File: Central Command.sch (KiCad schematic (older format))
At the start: 16 parts, among them P1 CONN_01X06, P2 CONN_01X02, U1 STM32F030C8, U2 MCP1700T-3302E/TT_

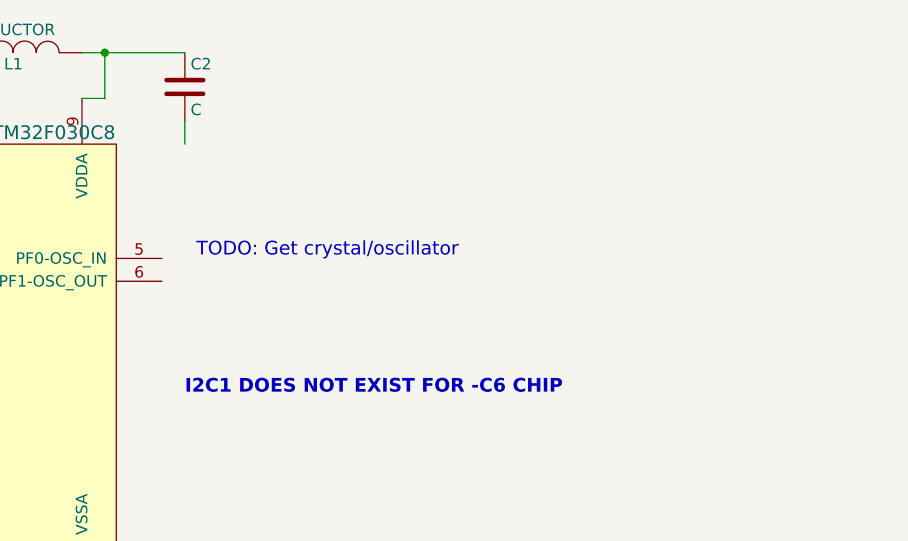
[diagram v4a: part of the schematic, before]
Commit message: Added Crystal to the schematic and layout
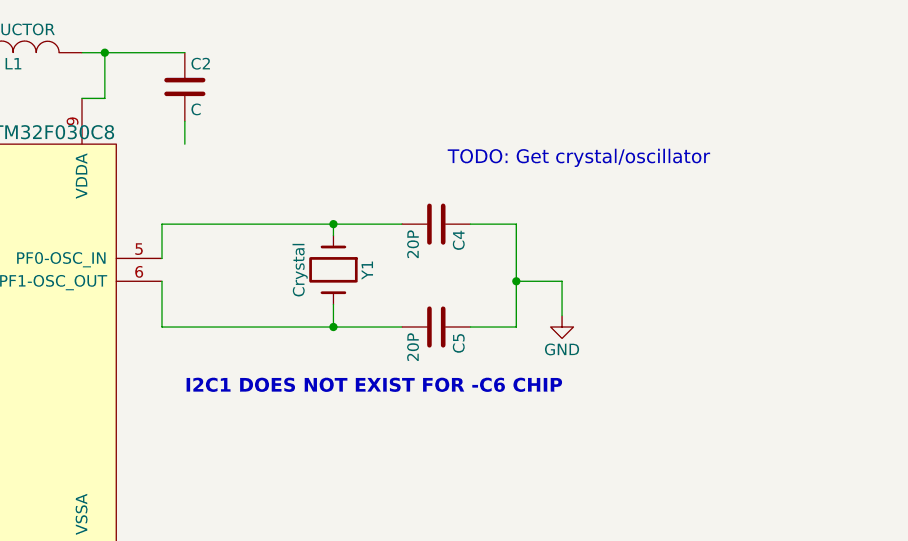
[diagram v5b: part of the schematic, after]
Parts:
- added C4, C5: 20P, Capacitors_SMD:C_0805, symbol C
- added Y1: Crystal, Crystals:Crystal_HC49-U_Vertical, symbol Crystal
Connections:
- wire segments 57 -> 68
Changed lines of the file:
@@
 	-1   0    0    -1
 $EndComp
-Wire Wire Line
-	7550 800  8000 800
-Wire Wire Line
-	7550 1000 7650 1000
-Wire Wire Line
-	7650 1000 7650 800
-Connection ~ 7650 800
-Wire Wire Line
-	8000 1100 8000 1200
-Wire Wire Line
-	6300 800  6950 800
-Wire Wire Line
-	6700 800  6700 1000
-Wire Wire Line
-	6800 800  6800 1000
-Connection ~ 6800 800
-Wire Wire Line
-	6900 1000 6900 900
-Wire Wire Line
-	6900 900  6800 900
-Connection ~ 6800 900
-Wire Wire Line
-	9050 4850 9050 5200
-Wire Wire Line
-	9050 5000 10150 5000
-Wire Wire Line
-	10150 5000 10150 4650
-Connection ~ 9050 5000
-Wire Wire Line
-	9050 5100 7900 5100
-Wire Wire Line
-	7900 5100 7900 4600
-Connection ~ 9050 5100
-Wire Wire Line
-	7300 4050 8300 4050
-Wire Wire Line
-	7900 4300 7900 4050
-Wire Wire Line
-	7900 4050 7950 4050
-Connection ~ 7950 4050
-Wire Wire Line
-	9800 4050 10600 4050
-Wire Wire Line
-	10150 4050 10150 4350
-Connection ~ 10150 4050
-Wire Wire Line
-	10750 4100 10600 4100
-Wire Wire Line
-	10600 4100 10600 4050
-Connection ~ 6700 800
-Wire Wire Line
-	6800 3150 6800 3300
-Wire Wire Line
-	6800 3250 7550 3250
-Wire Wire Line
-	6900 3250 6900 3150
-Connection ~ 6800 3250
-Wire Wire Line
-	7550 3250 7550 3150
-Connection ~ 6900 3250
-Wire Wire Line
-	5200 2500 6100 2500
-Wire Wire Line
-	5700 2500 5700 2600
-Wire Wire Line
-	5700 2900 5700 3100
-Wire Wire Line
-	5450 2600 5450 2500
-Connection ~ 5700 2500
-Wire Wire Line
-	5200 2600 5200 2500
-Connection ~ 5450 2500
-Wire Wire Line
-	1500 2500 3050 2500
-Wire Wire Line
-	1500 2500 1500 2800
-Wire Wire Line
-	1500 2800 750  2800
 Text GLabel 1900 1900 2    60   Input ~ 0
 3V3
-Wire Wire Line
-	850  1900 1900 1900
-Wire Wire Line
-	850  1900 850  2100
 $Comp
 L R R2
@@
 	1    0    0    -1
 $EndComp
-Wire Wire Line
-	850  2400 850  2500
-Wire Wire Line
-	850  2500 750  2500
 $Comp
 L GND #PWR03
@@
 	1    0    0    -1
 $EndComp
-Wire Wire Line
-	1000 2700 1000 3200
-Wire Wire Line
-	1000 2700 750  2700
-Wire Wire Line
-	750  2900 850  2900
-Wire Wire Line
-	850  2900 850  3600
 Text GLabel 1050 3600 2    60   Input ~ 0
 NRST
-Wire Wire Line
-	850  3600 1050 3600
 Text GLabel 6100 2850 0    60   Input ~ 0
 NRST
-Wire Wire Line
-	6100 2650 6100 2850
 $Comp
 L R R4
@@
 	1    0    0    -1
 $EndComp
-Wire Wire Line
-	1650 2400 1650 2500
-Connection ~ 1650 2500
-Wire Wire Line
-	1650 2100 1650 1900
-Connection ~ 1650 1900
-Wire Wire Line
-	1850 3050 1850 3150
-Wire Wire Line
-	1850 3150 1000 3150
-Connection ~ 1000 3150
-Wire Wire Line
-	1850 2600 1850 2750
-Wire Wire Line
-	750  2600 3050 2600
-Connection ~ 1850 2600
 $Comp
 L R R1
@@
 	1    0    0    -1
 $EndComp
-Wire Wire Line
-	750  3200 750  3000
-Wire Wire Line
-	750  3500 750  4000
-Wire Wire Line
-	750  4000 1050 4000
 Text GLabel 1050 4000 2    60   Input ~ 0
 TRACE
@@
 	0    1    1    0
 $EndComp
-Wire Wire Line
-	2850 2000 3050 2000
 $Comp
 L CONN_01X02 P2
@@
 	-1   0    0    -1
 $EndComp
-Wire Wire Line
-	2550 2000 2550 1400
-Wire Wire Line
-	2550 1400 2200 1400
-Wire Wire Line
-	2200 1500 2350 1500
-Wire Wire Line
-	2350 1500 2350 1650
 $Comp
 L GND #PWR04
@@
 	1    0    0    -1
 $EndComp
-Text Notes 8050 1700 0    60   ~ 0
+Text Notes 9150 1300 0    60   ~ 0
 TODO: Get crystal/oscillator
 Text Notes 2550 3100 0    60   ~ 0
@@
 Text Notes 5150 5700 0    60   ~ 0
 TODO: Determine if USB could be used for serial comm (ask Ron)
+$Comp
+L Crystal Y1
+U 1 1 56529888
+P 8650 1750
+F 0 "Y1" H 8650 1900 50  0000 C CNN
+F 1 "Crystal" H 8650 1600 50  0000 C CNN
+F 2 "Crystals:Crystal_HC49-U_Vertical" H 8650 1750 60  0001 C CNN
+F 3 "" H 8650 1750 60  0000 C CNN
+F 4 "http://parts.io/detail/343558/FOXSLF%2F080-20" H 8650 1750 60  0001 C CNN "Link"
+	1    8650 1750
+	0    1    1    0
+$EndComp
+$Comp
+L C C4
+U 1 1 5652990D
+P 9100 1550
+F 0 "C4" H 9125 1650 50  0000 L CNN
+F 1 "20P" H 9125 1450 50  0000 L CNN
+F 2 "Capacitors_SMD:C_0805" H 9138 1400 30  0001 C CNN
+F 3 "" H 9100 1550 60  0000 C CNN
+	1    9100 1550
+	0    1    1    0
+$EndComp
+$Comp
+L C C5
+U 1 1 56529966
+P 9100 2000
+F 0 "C5" H 9125 2100 50  0000 L CNN
+F 1 "20P" H 9125 1900 50  0000 L CNN
+F 2 "Capacitors_SMD:C_0805" H 9138 1850 30  0001 C CNN
+F 3 "" H 9100 2000 60  0000 C CNN
+	1    9100 2000
+	0    1    1    0
+$EndComp
+$Comp
+L GND #PWR05
+U 1 1 56529BFD
+P 9650 1950
+F 0 "#PWR05" H 9650 1700 50  0001 C CNN
+F 1 "GND" H 9650 1800 50  0000 C CNN
+F 2 "" H 9650 1950 60  0000 C CNN
+F 3 "" H 9650 1950 60  0000 C CNN
+	1    9650 1950
+	1    0    0    -1
+$EndComp
+Wire Wire Line
+	7550 800  8000 800
+Wire Wire Line
+	7550 1000 7650 1000
+Wire Wire Line
+	7650 1000 7650 800
+Connection ~ 7650 800
+Wire Wire Line
+	8000 1100 8000 1200
+Wire Wire Line
+	6300 800  6950 800
+Wire Wire Line
+	6700 800  6700 1000
+Wire Wire Line
+	6800 800  6800 1000
+Connection ~ 6800 800
+Wire Wire Line
+	6900 1000 6900 900
+Wire Wire Line
+	6900 900  6800 900
+Connection ~ 6800 900
+Wire Wire Line
+	9050 4850 9050 5200
+Wire Wire Line
+	9050 5000 10150 5000
+Wire Wire Line
+	10150 5000 10150 4650
+Connection ~ 9050 5000
+Wire Wire Line
+	9050 5100 7900 5100
+Wire Wire Line
+	7900 5100 7900 4600
+Connection ~ 9050 5100
+Wire Wire Line
+	7300 4050 8300 4050
+Wire Wire Line
+	7900 4300 7900 4050
+Wire Wire Line
+	7900 4050 7950 4050
+Connection ~ 7950 4050
+Wire Wire Line
+	9800 4050 10600 4050
+Wire Wire Line
+	10150 4050 10150 4350
+Connection ~ 10150 4050
+Wire Wire Line
+	10750 4100 10600 4100
+Wire Wire Line
+	10600 4100 10600 4050
+Connection ~ 6700 800
+Wire Wire Line
+	6800 3150 6800 3300
+Wire Wire Line
+	6800 3250 7550 3250
+Wire Wire Line
+	6900 3250 6900 3150
+Connection ~ 6800 3250
+Wire Wire Line
+	7550 3250 7550 3150
+Connection ~ 6900 3250
+Wire Wire Line
+	5200 2500 6100 2500
+Wire Wire Line
+	5700 2500 5700 2600
+Wire Wire Line
+	5700 2900 5700 3100
+Wire Wire Line
+	5450 2600 5450 2500
+Connection ~ 5700 2500
+Wire Wire Line
+	5200 2600 5200 2500
+Connection ~ 5450 2500
+Wire Wire Line
+	1500 2500 3050 2500
+Wire Wire Line
+	1500 2500 1500 2800
+Wire Wire Line
+	1500 2800 750  2800
+Wire Wire Line
+	850  1900 1900 1900
+Wire Wire Line
+	850  1900 850  2100
+Wire Wire Line
+	850  2400 850  2500
+Wire Wire Line
+	850  2500 750  2500
+Wire Wire Line
+	1000 2700 1000 3200
+Wire Wire Line
+	1000 2700 750  2700
+Wire Wire Line
+	750  2900 850  2900
+Wire Wire Line
+	850  2900 850  3600
+Wire Wire Line
+	850  3600 1050 3600
+Wire Wire Line
+	6100 2650 6100 2850
+Wire Wire Line
+	1650 2400 1650 2500
+Connection ~ 1650 2500
+Wire Wire Line
+	1650 2100 1650 1900
+Connection ~ 1650 1900
+Wire Wire Line
+	1850 3050 1850 3150
+Wire Wire Line
+	1850 3150 1000 3150
+Connection ~ 1000 3150
+Wire Wire Line
+	1850 2600 1850 2750
+Wire Wire Line
+	750  2600 3050 2600
+Connection ~ 1850 2600
+Wire Wire Line
+	750  3200 750  3000
+Wire Wire Line
+	750  3500 750  4000
+Wire Wire Line
+	750  4000 1050 4000
+Wire Wire Line
+	2850 2000 3050 2000
+Wire Wire Line
+	2550 2000 2550 1400
+Wire Wire Line
+	2550 1400 2200 1400
+Wire Wire Line
+	2200 1500 2350 1500
+Wire Wire Line
+	2350 1500 2350 1650
+Wire Wire Line
+	8950 1550 7900 1550
+Wire Wire Line
+	7900 1550 7900 1700
+Wire Wire Line
+	8650 1600 8650 1550
+Connection ~ 8650 1550
+Wire Wire Line
+	9250 1550 9450 1550
+Wire Wire Line
+	9450 1550 9450 2000
+Wire Wire Line
+	9450 2000 9250 2000
+Wire Wire Line
+	9450 1800 9650 1800
+Wire Wire Line
+	9650 1800 9650 1950
+Connection ~ 9450 1800
+Wire Wire Line
+	8950 2000 7900 2000
+Wire Wire Line
+	7900 2000 7900 1800
+Wire Wire Line
+	8650 1900 8650 2000
+Connection ~ 8650 2000
 $EndSCHEMATC

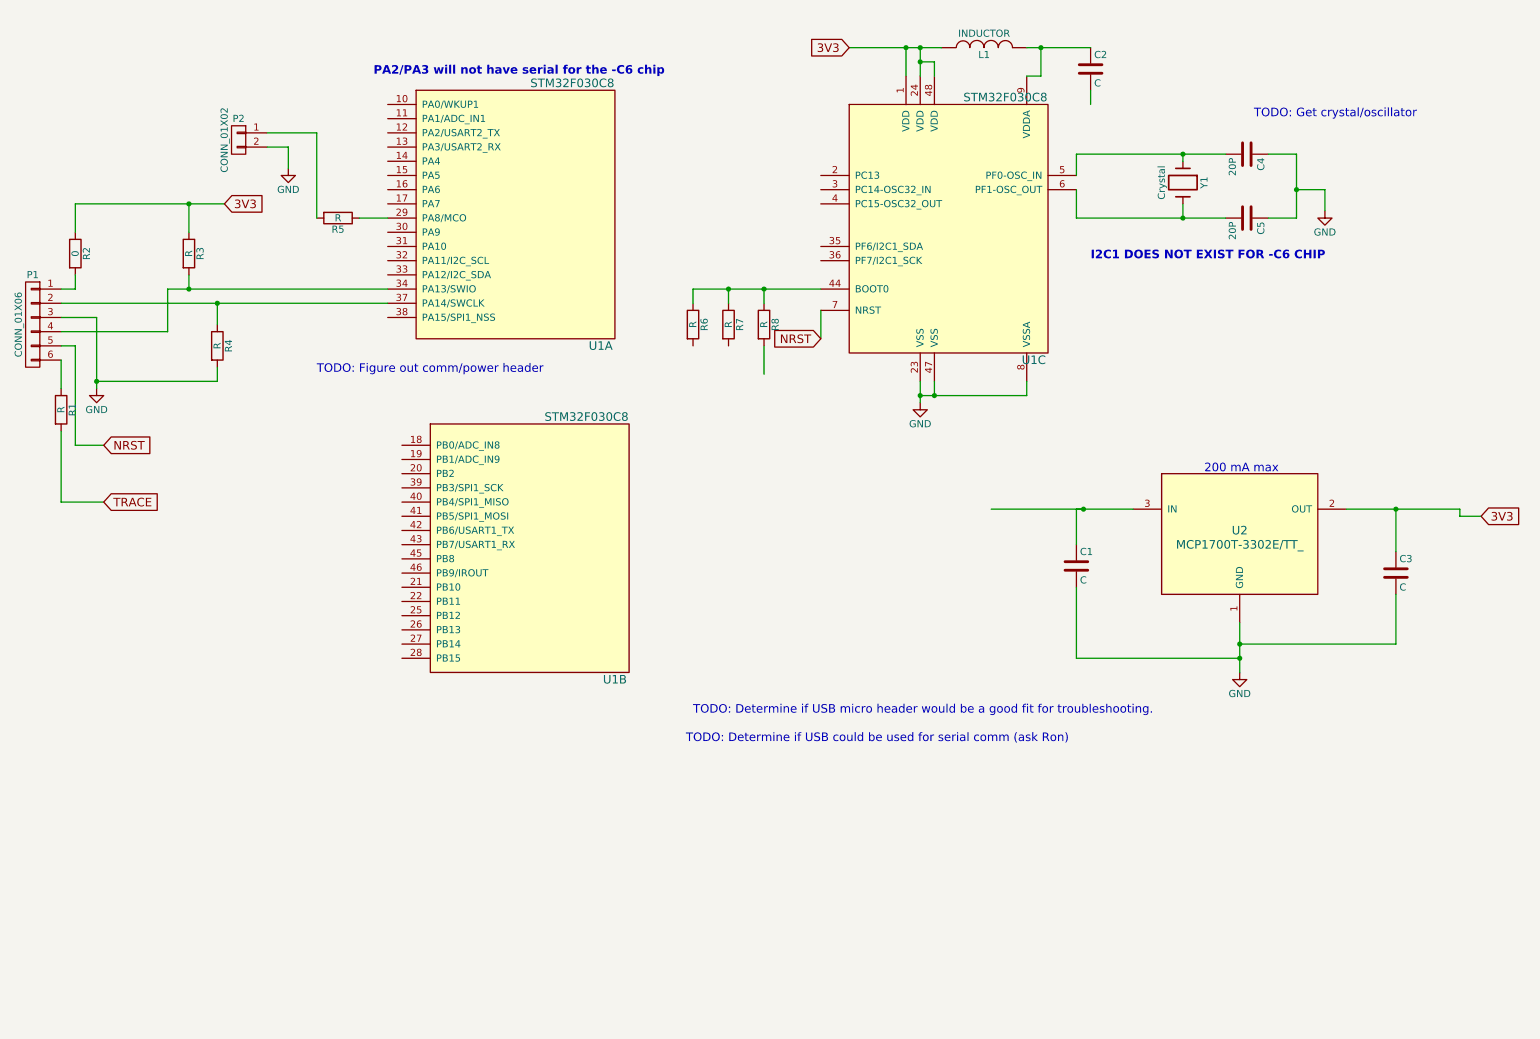
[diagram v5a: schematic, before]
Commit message: Changed BOOT0 pin hookup, added reset button
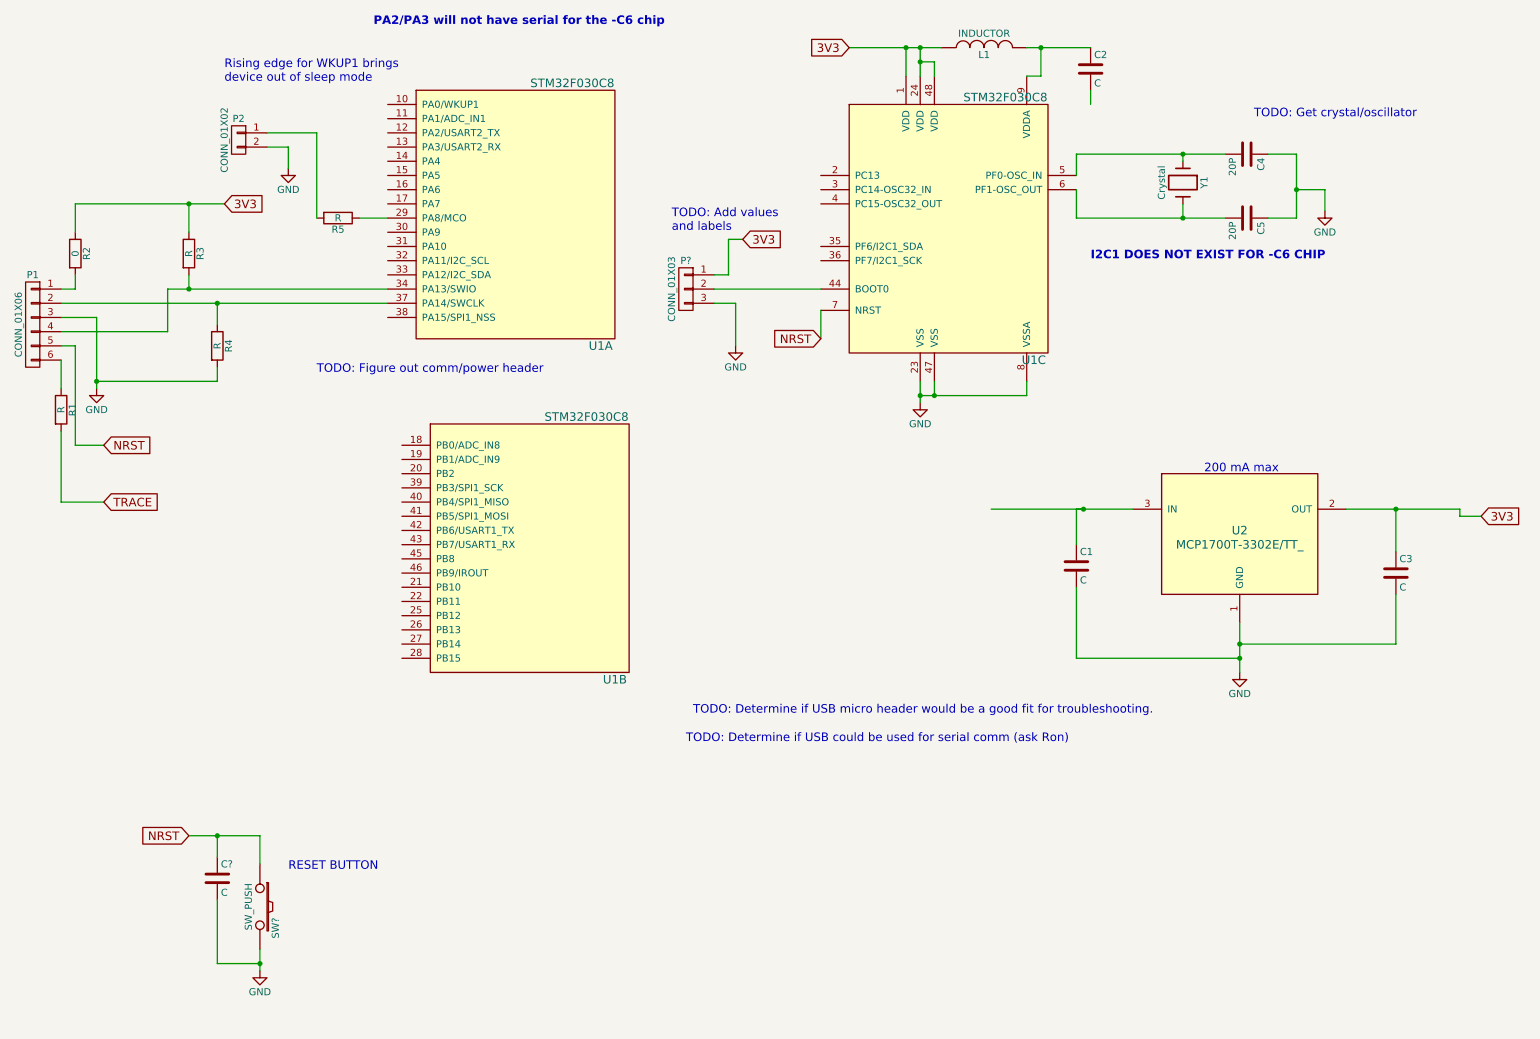
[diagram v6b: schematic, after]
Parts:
- removed R6, R7, R8: R, Resistors_SMD:R_0805, symbol R
- added C?: C, symbol C
- added P?: CONN_01X03, symbol CONN_01X03
- added SW?: SW_PUSH, symbol SW_PUSH
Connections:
- wire segments 68 -> 75
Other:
- note added: "RESET BUTTON"
- note added: "Rising edge for WKUP1 brings \ndevice out of sleep mode"
- note added: "TODO: Add values \nand labels"
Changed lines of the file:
@@
 200 mA max
-$Comp
-L R R8
-U 1 1 562D2D9E
-P 5700 2750
-F 0 "R8" V 5780 2750 50  0000 C CNN
-F 1 "R" V 5700 2750 50  0000 C CNN
-F 2 "Resistors_SMD:R_0805" V 5630 2750 30  0001 C CNN
-F 3 "" H 5700 2750 30  0000 C CNN
-	1    5700 2750
-	1    0    0    -1
-$EndComp
-$Comp
-L R R7
-U 1 1 562D2E53
-P 5450 2750
-F 0 "R7" V 5530 2750 50  0000 C CNN
-F 1 "R" V 5450 2750 50  0000 C CNN
-F 2 "Resistors_SMD:R_0805" V 5380 2750 30  0001 C CNN
-F 3 "" H 5450 2750 30  0000 C CNN
-	1    5450 2750
-	1    0    0    -1
-$EndComp
-$Comp
-L R R6
-U 1 1 562D2EC7
-P 5200 2750
-F 0 "R6" V 5280 2750 50  0000 C CNN
-F 1 "R" V 5200 2750 50  0000 C CNN
-F 2 "Resistors_SMD:R_0805" V 5130 2750 30  0001 C CNN
-F 3 "" H 5200 2750 30  0000 C CNN
-	1    5200 2750
-	1    0    0    -1
-$EndComp
 $Comp
 L CONN_01X06 P1
@@
 	1    0    0    -1
 $EndComp
-Text Notes 2950 1000 0    60   ~ 12
+Text Notes 2950 650  0    60   ~ 12
 PA2/PA3 will not have serial for the -C6 chip
 $Comp
@@
 Connection ~ 6900 3250
 Wire Wire Line
-	5200 2500 6100 2500
-Wire Wire Line
-	5700 2500 5700 2600
-Wire Wire Line
-	5700 2900 5700 3100
-Wire Wire Line
-	5450 2600 5450 2500
-Connection ~ 5700 2500
-Wire Wire Line
-	5200 2600 5200 2500
-Connection ~ 5450 2500
-Wire Wire Line
 	1500 2500 3050 2500
 Wire Wire Line
@@
 	8650 1900 8650 2000
 Connection ~ 8650 2000
+Text GLabel 1650 6350 0    60   Input ~ 0
+NRST
+Wire Wire Line
+	1650 6350 2150 6350
+Wire Wire Line
+	2150 6350 2150 6550
+$Comp
+L C C?
+U 1 1 5652BD44
+P 1850 6650
+F 0 "C?" H 1875 6750 50  0000 L CNN
+F 1 "C" H 1875 6550 50  0000 L CNN
+F 2 "" H 1888 6500 30  0000 C CNN
+F 3 "" H 1850 6650 60  0000 C CNN
+	1    1850 6650
+	1    0    0    -1
+$EndComp
+Wire Wire Line
+	1850 6500 1850 6350
+Connection ~ 1850 6350
+$Comp
+L SW_PUSH SW?
+U 1 1 5652C03C
+P 2150 6850
+F 0 "SW?" H 2300 6960 50  0000 C CNN
+F 1 "SW_PUSH" H 2150 6770 50  0000 C CNN
+F 2 "" H 2150 6850 60  0000 C CNN
+F 3 "" H 2150 6850 60  0000 C CNN
+	1    2150 6850
+	0    1    1    0
+$EndComp
+$Comp
+L GND #PWR?
+U 1 1 5652C33A
+P 2150 7300
+F 0 "#PWR?" H 2150 7050 50  0001 C CNN
+F 1 "GND" H 2150 7150 50  0000 C CNN
+F 2 "" H 2150 7300 60  0000 C CNN
+F 3 "" H 2150 7300 60  0000 C CNN
+	1    2150 7300
+	1    0    0    -1
+$EndComp
+Wire Wire Line
+	2150 7150 2150 7300
+Wire Wire Line
+	2150 7250 1850 7250
+Wire Wire Line
+	1850 7250 1850 6800
+Connection ~ 2150 7250
+Text Notes 2350 6600 0    60   ~ 0
+RESET BUTTON
+Text Notes 5050 2100 0    60   ~ 0
+TODO: Add values \nand labels
+$Comp
+L CONN_01X03 P?
+U 1 1 5652DAE0
+P 5150 2500
+F 0 "P?" H 5150 2700 50  0000 C CNN
+F 1 "CONN_01X03" V 5250 2500 50  0000 C CNN
+F 2 "" H 5150 2500 60  0000 C CNN
+F 3 "" H 5150 2500 60  0000 C CNN
+	1    5150 2500
+	-1   0    0    -1
+$EndComp
+Wire Wire Line
+	5350 2500 6100 2500
+Wire Wire Line
+	5350 2600 5500 2600
+Wire Wire Line
+	5500 2600 5500 2900
+$Comp
+L GND #PWR?
+U 1 1 5652DC74
+P 5500 2900
+F 0 "#PWR?" H 5500 2650 50  0001 C CNN
+F 1 "GND" H 5500 2750 50  0000 C CNN
+F 2 "" H 5500 2900 60  0000 C CNN
+F 3 "" H 5500 2900 60  0000 C CNN
+	1    5500 2900
+	1    0    0    -1
+$EndComp
+Text GLabel 5550 2150 2    60   Input ~ 0
+3V3
+Wire Wire Line
+	5550 2150 5450 2150
+Wire Wire Line
+	5450 2150 5450 2400
+Wire Wire Line
+	5450 2400 5350 2400
+Text Notes 1900 1050 0    60   ~ 0
+Rising edge for WKUP1 brings \ndevice out of sleep mode
 $EndSCHEMATC
